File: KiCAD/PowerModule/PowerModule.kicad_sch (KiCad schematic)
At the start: 38 parts, among them J1 GPU, J2 DF1B-2S-2.5R, J3 DF1B-2S-2.5R, J4 DF1B-2S-2.5R, J5 BUS, J6 MASTER, J7 MONITOR, Q1 AO3401A, Q2 AO3401A, U1 INA219BxDCN, U2 INA219BxDCN, U4 INA219BxDCN

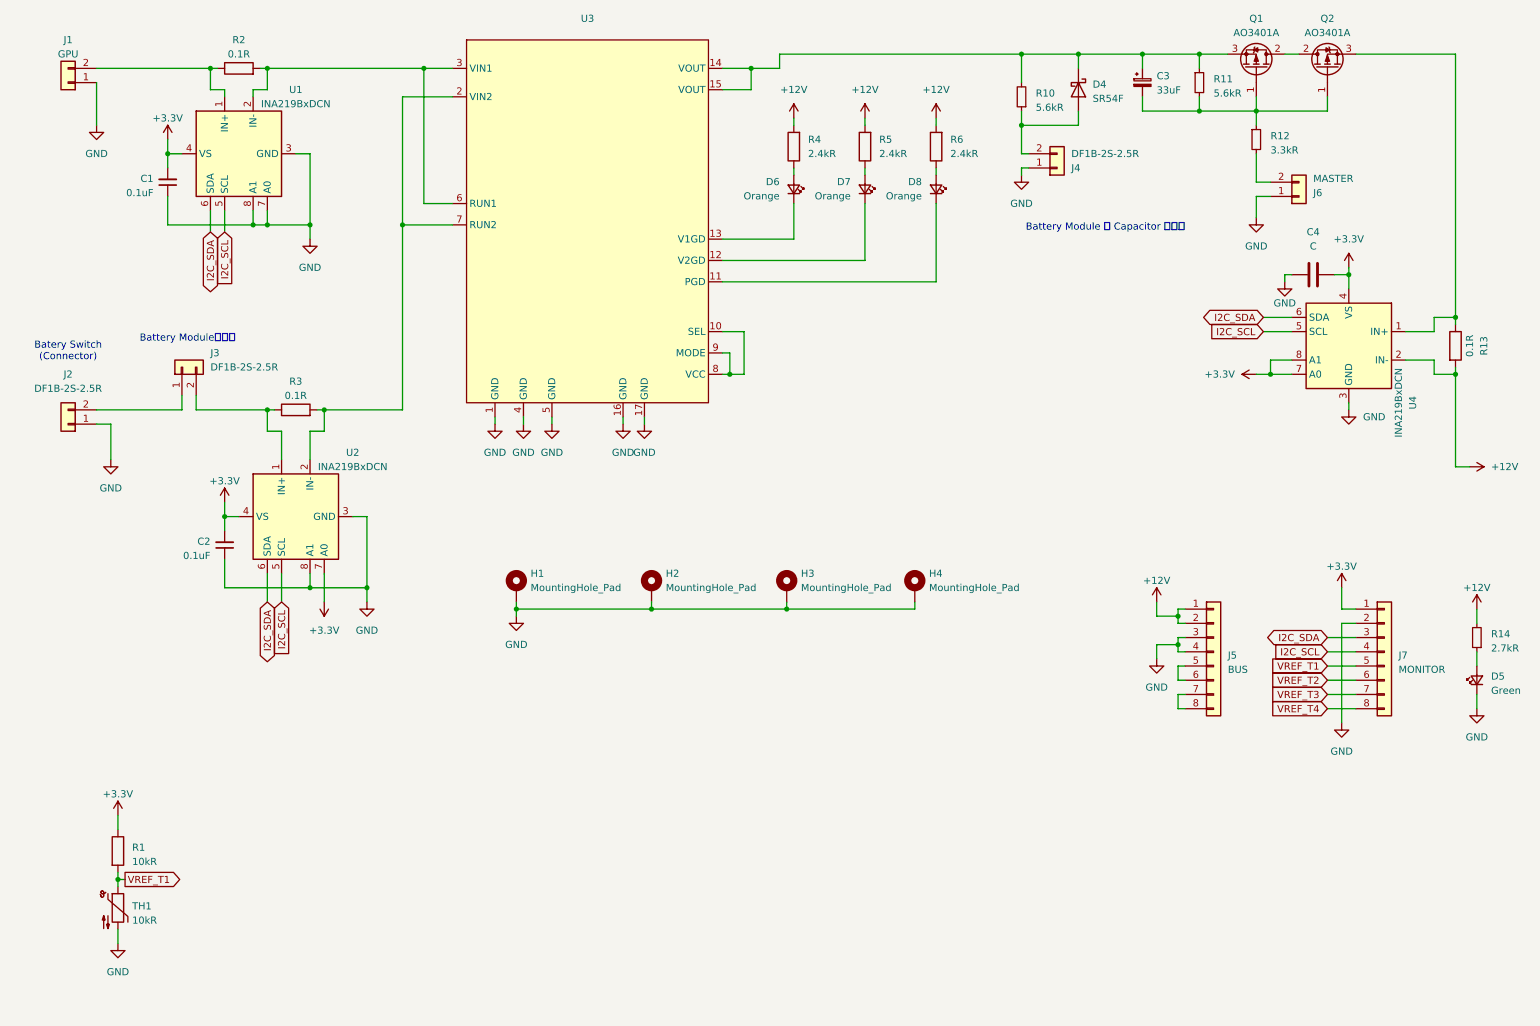
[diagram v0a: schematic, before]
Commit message: 3Dモデルを組み合わせて結合試験する
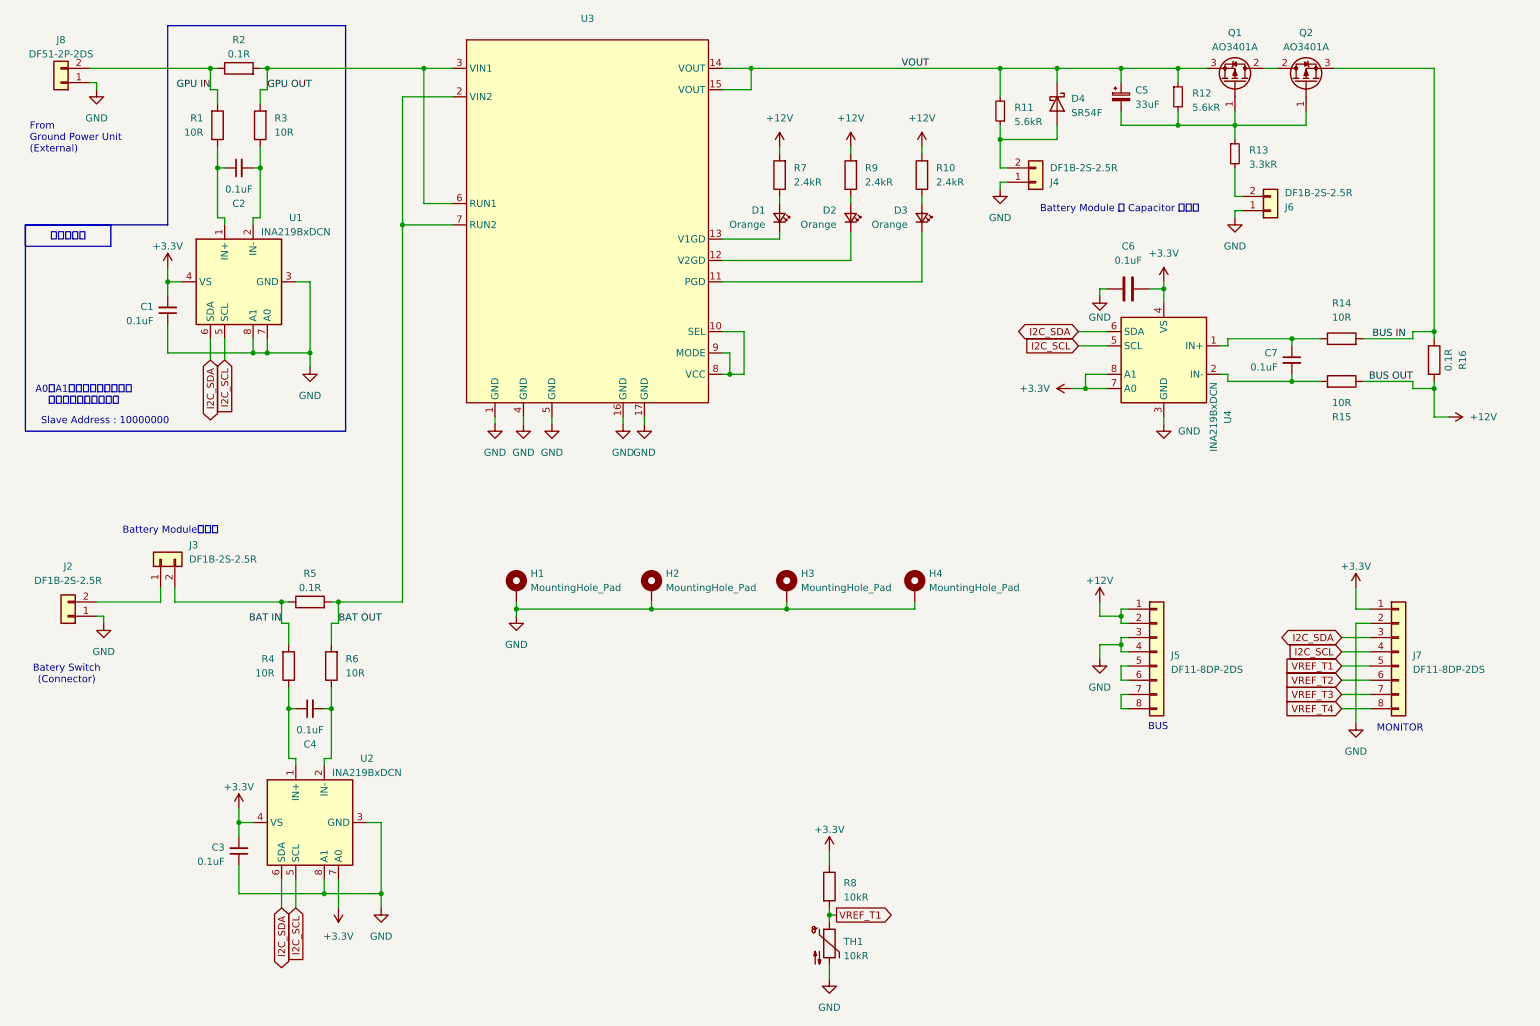
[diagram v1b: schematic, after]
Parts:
- removed D5: Green, LED_SMD:LED_0603_1608Metric_Pad1.05x0.95mm_HandSolder, symbol Device:LED_Small
- removed J1: GPU, TSRP_Connector_Hirose:DF1B-2S-2.5R, symbol Connector_Generic:Conn_01x02
- removed R14: 2.7kR, Resistor_SMD:R_0603_1608Metric_Pad0.98x0.95mm_HandSolder, symbol Device:R_Small
- added C2, C4: 0.1uF, Capacitor_SMD:C_0603_1608Metric_Pad1.08x0.95mm_HandSolder, symbol Device:C_Small
- added C7: 0.1uF, Capacitor_SMD:C_0603_1608Metric, symbol Device:C_Small
- added J8: DF51-2P-2DS, TSRP_Connector_Hirose:DF51-2P-2DS, symbol Connector_Generic:Conn_01x02
- added R1, R14, R15, R3, R4, R6: 10R, Resistor_SMD:R_0603_1608Metric_Pad0.98x0.95mm_HandSolder, symbol Device:R
- C6: renamed from C4; value C -> 0.1uF; footprint (none) -> Capacitor_SMD:C_0603_1608Metric_Pad1.08x0.95mm_HandSolder
- H4: footprint MountingHole:MountingHole_3.2mm_M3_DIN965_Pad_TopBottom -> MountingHole:MountingHole_3.2mm_M3_ISO7380_Pad_TopBottom
- J5: value BUS -> DF11-8DP-2DS
- J6: value MASTER -> DF1B-2S-2.5R
- J7: value MONITOR -> DF11-8DP-2DS
- renumbered C2 to C3, C3 to C5, D6 to D1, D7 to D2, D8 to D3, R6 to R10, R10 to R11, R11 to R12, R12 to R13, R13 to R16, R3 to R5, R4 to R7, R1 to R8, R5 to R9
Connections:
- net +12V: now also R15.1; no longer U4.2 (IN-)
- net GND: now also J8.1 (Pin_1)
- net VOUT: now reaches C5.1, D4.1 (K), Q1.3 (S), R11.2, R12.1, U3.14 (VOUT), U3.15 (VOUT)
- net at U1.1 (IN+): now also C2.1, R1.1; no longer R2.1
- net BAT IN: now reaches J3.2 (Pin_2), R5.1
- net BAT IN: now also R4.2; no longer U2.1 (IN+)
- net BAT OUT: now reaches R5.2, U3.2 (VIN2), U3.7 (RUN2)
- net BAT OUT: now also R6.2; no longer U2.2 (IN-)
- net BUS IN: now reaches Q2.3 (S), R16.1
- net BUS IN: now also R14.2; no longer U4.1 (IN+)
- net GPU OUT: now reaches R2.2, U3.3 (VIN1), U3.6 (RUN1)
- net GPU OUT: now also R3.2; no longer U1.2 (IN-)
- new net: C2.2, R3.1, U1.2 (IN-)
- new net: C7.1, R14.1, U4.1 (IN+)
- new net: C7.2, R15.2, U4.2 (IN-)
- new net: C4.1, R4.1, U2.1 (IN+)
- new net: C4.2, R6.1, U2.2 (IN-)
- new net GPU IN: J8.2 (Pin_2), R1.2, R2.1
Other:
- note added: "A0とA1はスレーブアドレス を設定するためのピン"
- note added: "BUS"
- note added: "From Ground Power Unit (External)"
- note added: "MONITOR"
- note added: "Slave Address : 10000000"
- moved on the sheet: C1, C3, C5, C6, D1, D2, D3, D4, J2, J3, J4, J5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
